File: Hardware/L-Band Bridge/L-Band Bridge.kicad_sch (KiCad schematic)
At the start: 89 parts, among them J1 SMA, J2 SMA, J3 SMA, J4 Conn_02x08_Odd_Even, Q1 MMBT3904, U1 ADP-2-20+, U10 DBTC-17-5LX+, U3 LM358, U4 GALI-52, U5 GALI-52, U6 HMC472ALP4E, U7 ADE-17H+, U9 DBTC-17-5LX+

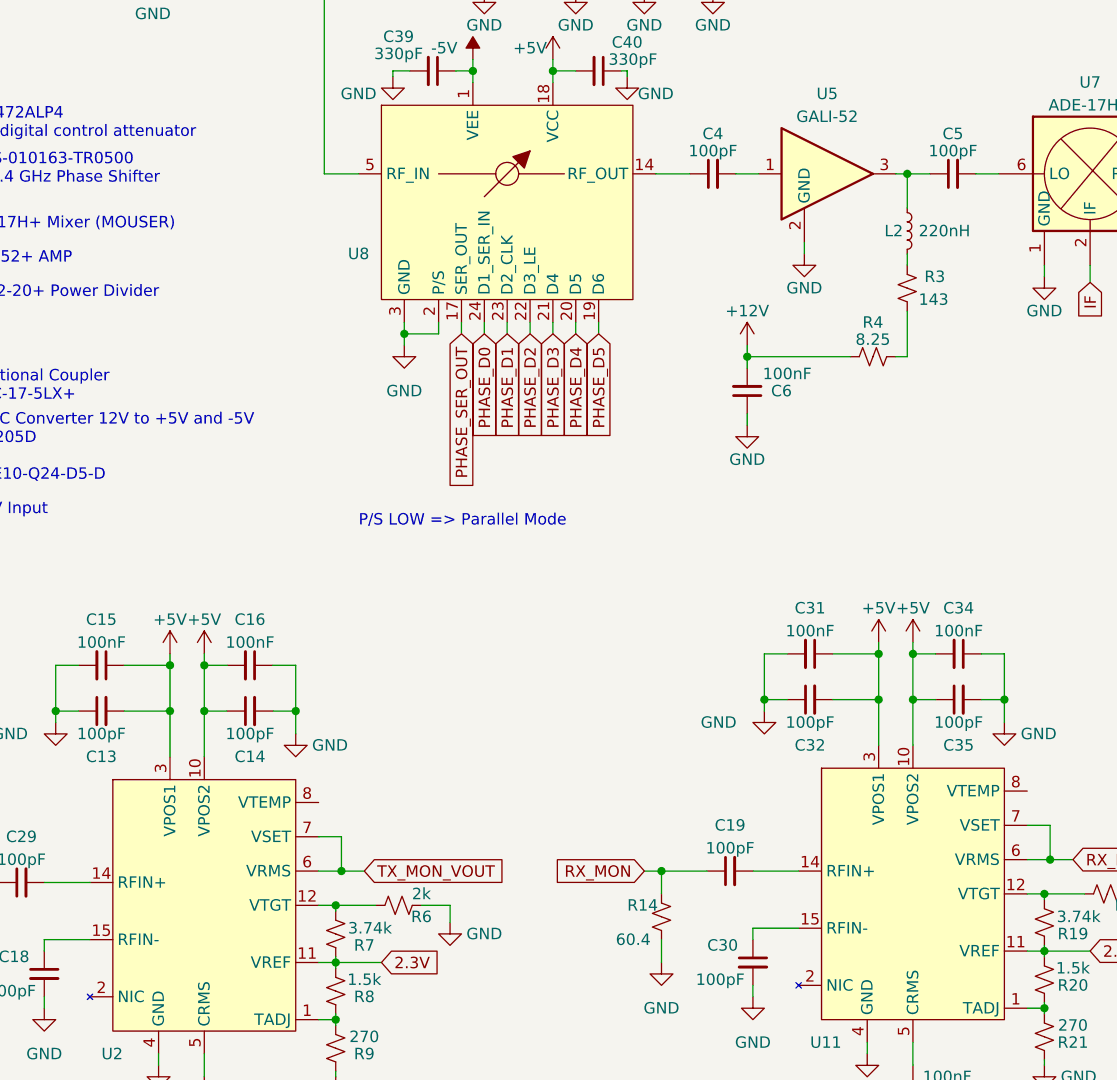
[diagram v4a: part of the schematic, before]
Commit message: Updating L-band bridge schematic
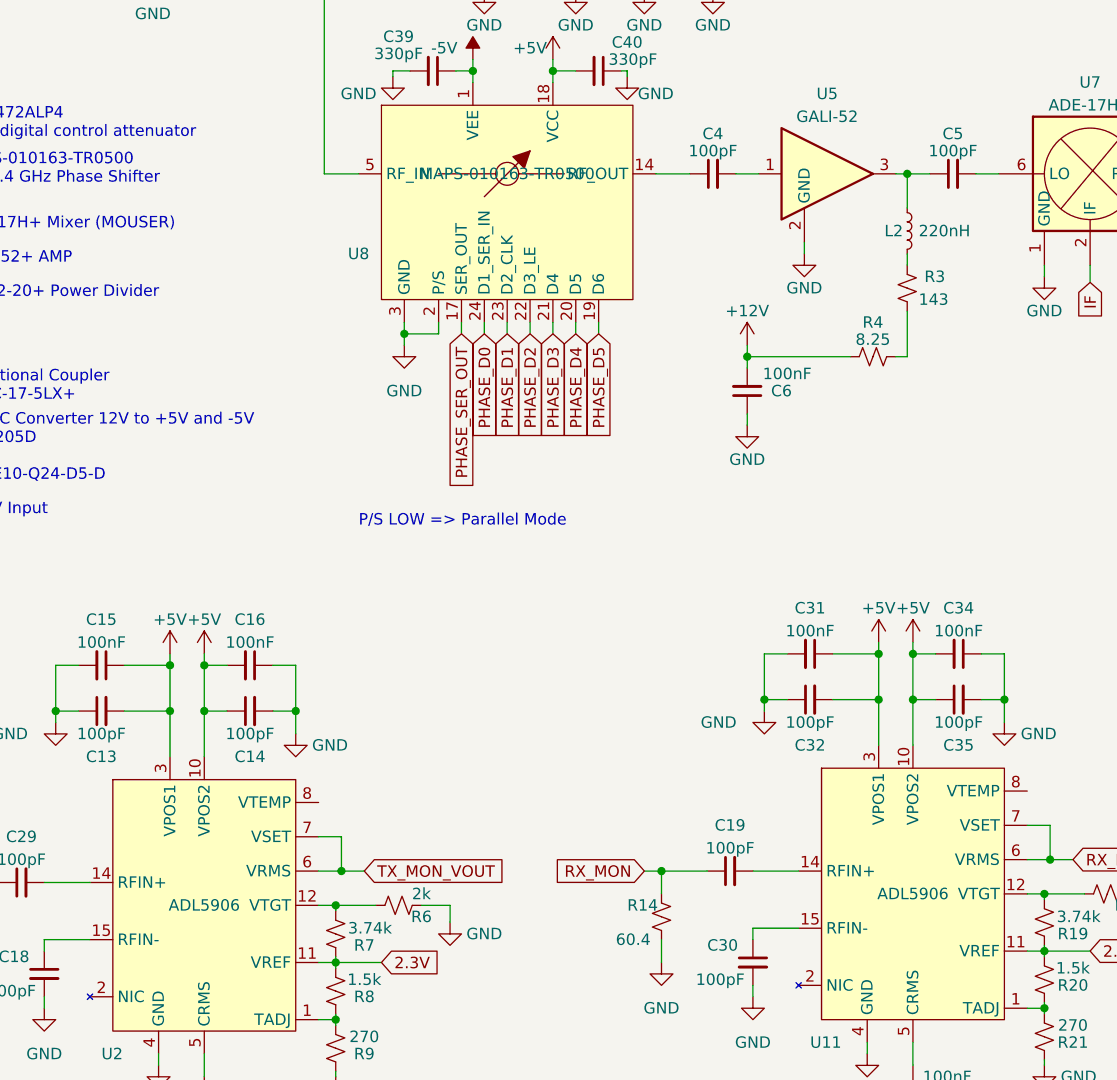
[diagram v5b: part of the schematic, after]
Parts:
- U10, U9: footprint (none) -> _tim-RF-Mini-Circuits:DBTC-17-5LX+
- U11, U2: value ~ -> ADL5906; footprint (none) -> Package_DFN_QFN:QFN-16-1EP_4x4mm_P0.65mm_EP2.1x2.1mm_ThermalVias
- U8: value ~ -> MAPS-010163-TR0500
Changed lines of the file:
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@@
       (effects (font (size 1.27 1.27)))
     )
-    (property "Footprint" "" (at 175.26 56.515 0)
+    (property "Footprint" "_tim-RF-Mini-Circuits:DBTC-17-5LX+" (at 175.26 56.515 0)
       (effects (font (size 1.27 1.27)) hide)
     )
@@
     )
   )
-  (symbol (lib_id "_tim-RF:DBTC-17-5LX+") (at 177.8 81.28 0) (mirror y) (unit 1)
+  (symbol (lib_name "DBTC-17-5LX+_1") (lib_id "_tim-RF:DBTC-17-5LX+") (at 177.8 81.28 0) (mirror y) (unit 1)
     (in_bom yes) (on_board yes) (dnp no)
     (property "Reference" "U10" (at 177.8 76.2 0)
@@
       (effects (font (size 1.27 1.27)))
     )
-    (property "Footprint" "" (at 177.8 95.885 0)
+    (property "Footprint" "_tim-RF-Mini-Circuits:DBTC-17-5LX+" (at 177.8 95.885 0)
       (effects (font (size 1.27 1.27)) hide)
     )
@@
       (effects (font (size 1.27 1.27)))
     )
-    (property "Value" "~" (at 86.36 81.28 0)
+    (property "Value" "MAPS-010163-TR0500" (at 86.36 81.28 0)
       (effects (font (size 1.27 1.27)))
     )
@@
     )
   )
-  (symbol (lib_id "_tim-RF:ADL5906") (at 131.445 161.29 0) (unit 1)
+  (symbol (lib_name "ADL5906_1") (lib_id "_tim-RF:ADL5906") (at 131.445 161.29 0) (unit 1)
     (in_bom yes) (on_board yes) (dnp no)
     (property "Reference" "U11" (at 120.015 177.8 0)
       (effects (font (size 1.27 1.27)) (justify left))
     )
-    (property "Value" "~" (at 131.445 161.29 0)
-      (effects (font (size 1.27 1.27)))
-    )
-    (property "Footprint" "" (at 131.445 161.29 0)
+    (property "Value" "ADL5906" (at 131.445 161.29 0)
+      (effects (font (size 1.27 1.27)))
+    )
+    (property "Footprint" "Package_DFN_QFN:QFN-16-1EP_4x4mm_P0.65mm_EP2.1x2.1mm_ThermalVias" (at 131.445 161.29 0)
       (effects (font (size 1.27 1.27)) hide)
     )
@@
       (effects (font (size 1.27 1.27)) (justify left))
     )
-    (property "Value" "~" (at 52.705 162.56 0)
-      (effects (font (size 1.27 1.27)))
-    )
-    (property "Footprint" "" (at 52.705 162.56 0)
-      (effects (font (size 1.27 1.27)) hide)
-    )
+    (property "Value" "ADL5906" (at 52.705 162.56 0)
+      (effects (font (size 1.27 1.27)))
+    )
+    (property "Footprint" "Package_DFN_QFN:QFN-16-1EP_4x4mm_P0.65mm_EP2.1x2.1mm_ThermalVias" (at 52.705 162.56 0)
+      (effects (font (size 1.27 1.27)) hide)
+    )

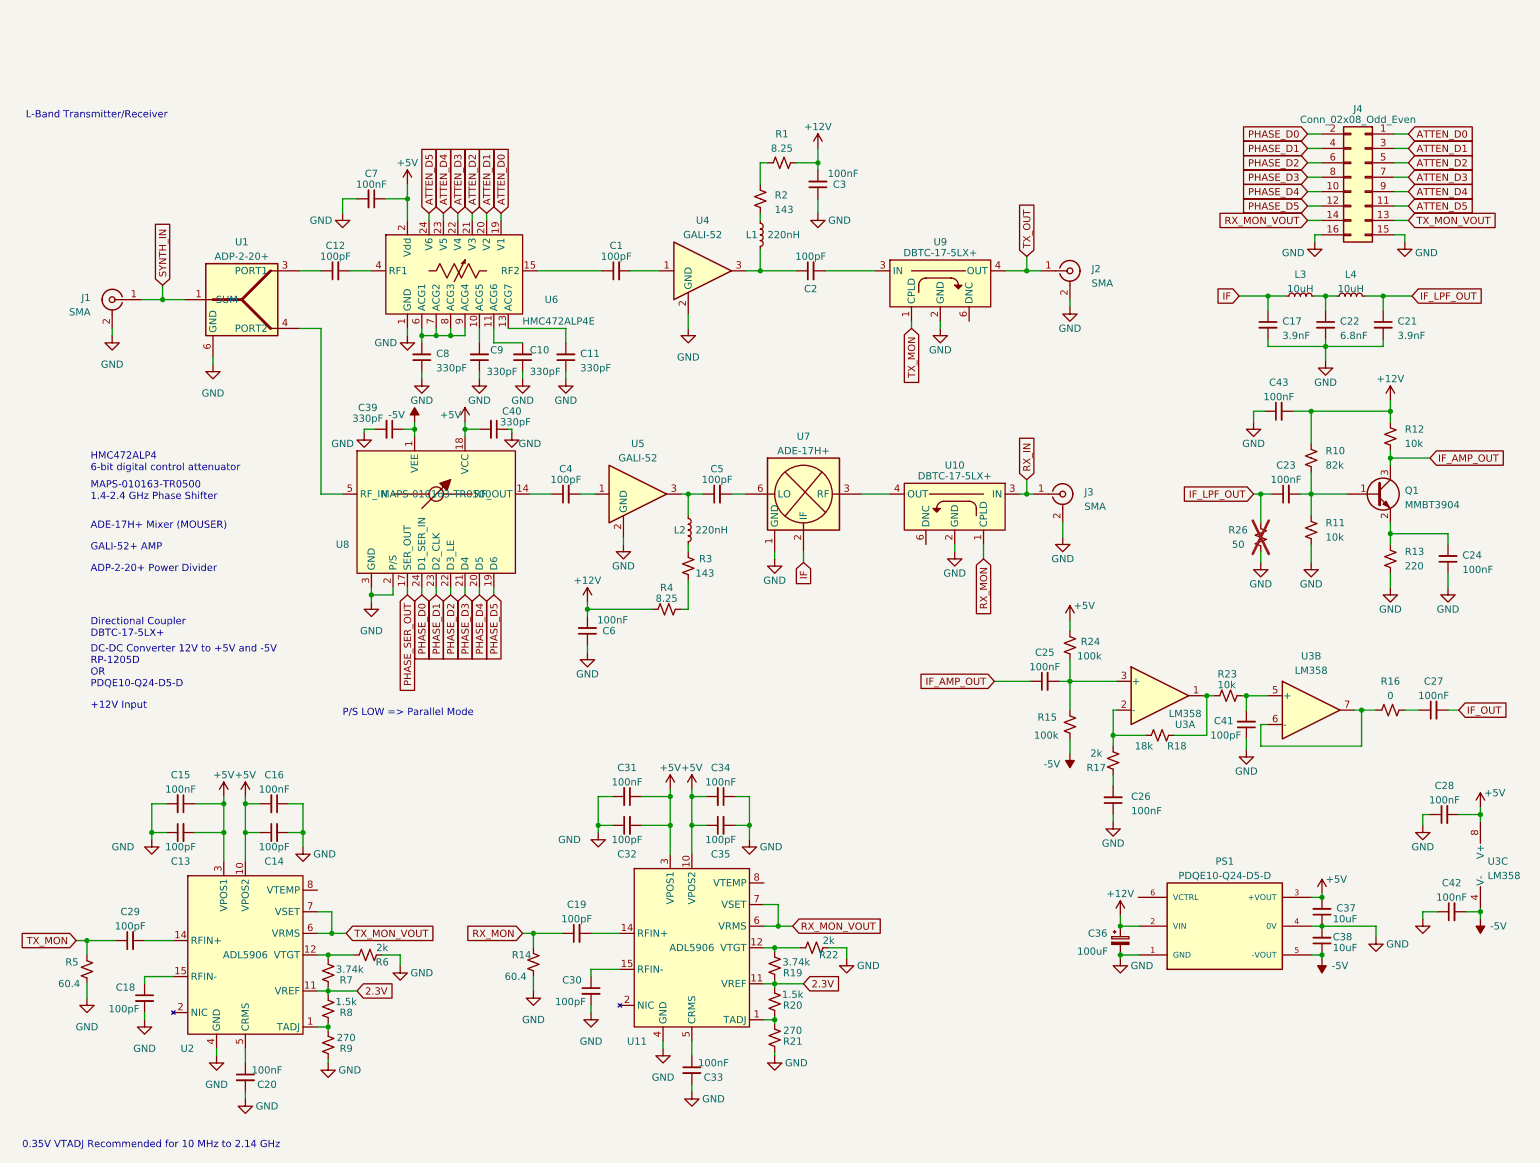
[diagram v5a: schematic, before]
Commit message: Updating Schematic
Removed Power Divider
Removed Op Amp on IF output
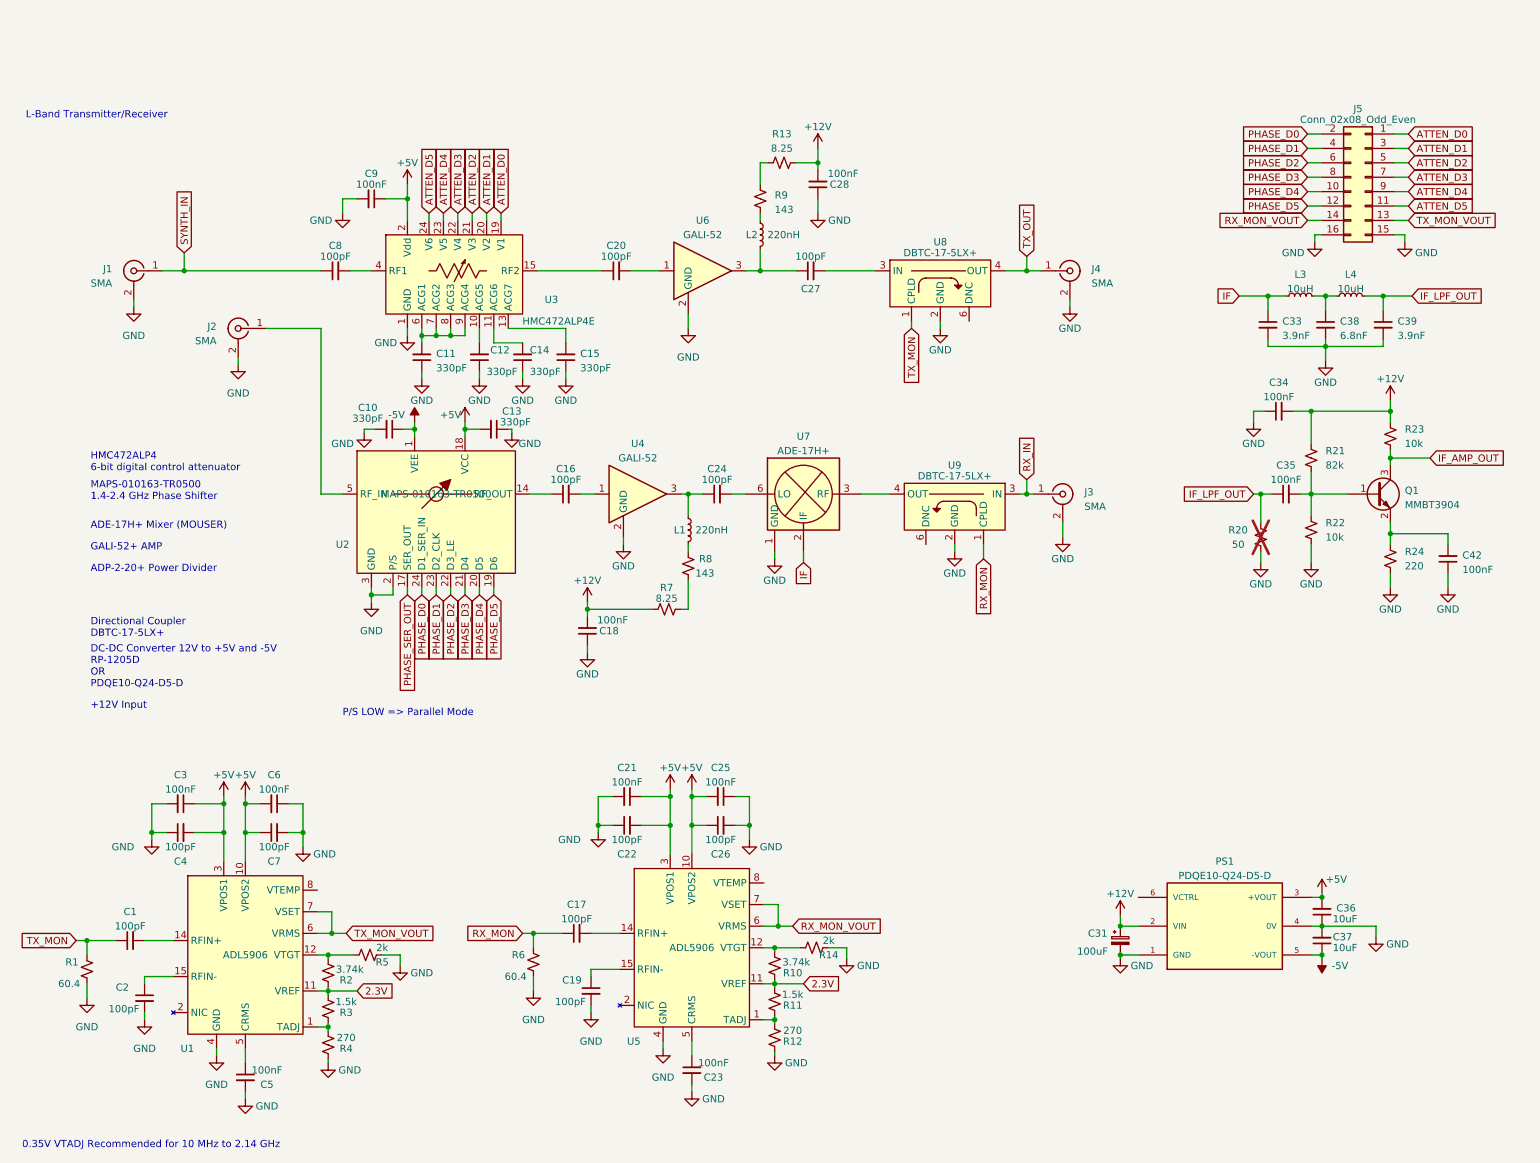
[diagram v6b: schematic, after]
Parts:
- removed C25, C26, C27, C28, C42: 100nF, Capacitor_SMD:C_0402_1005Metric, symbol Device:C_Small
- removed C41: 100pF, Capacitor_SMD:C_0402_1005Metric, symbol Device:C_Small
- removed R15: 100k, Resistor_SMD:R_0402_1005Metric, symbol Device:R_Small_US
- removed R16: 0, Capacitor_SMD:C_0402_1005Metric, symbol Device:R_Small_US
- removed R17: 2k, Capacitor_SMD:C_0402_1005Metric, symbol Device:R_Small_US
- removed R18: 18k, Capacitor_SMD:C_0402_1005Metric, symbol Device:R_Small_US
- removed R23: 10k, Capacitor_SMD:C_0402_1005Metric, symbol Device:R_Small_US
- removed R24: 100k, Capacitor_SMD:C_0402_1005Metric, symbol Device:R_Small_US
- removed U1: ADP-2-20+, RF_Mini-Circuits:Mini-Circuits_CD636_LandPatternPL-035, symbol _tim-RF:ADP-2-20+
- removed U3: LM358, Package_SO:MSOP-8_3x3mm_P0.65mm, symbol Amplifier_Operational:LM358
- added J2: SMA, Connector_Coaxial:SMA_Amphenol_132291_Vertical, symbol Connector:Conn_Coaxial
- renumbered C29 to C1, C39 to C10, C8 to C11, C9 to C12, C40 to C13, C10 to C14, C11 to C15, C4 to C16, C19 to C17, C6 to C18, C30 to C19, C18 to C2, C1 to C20, C31 to C21, C32 to C22, C33 to C23, C5 to C24, C34 to C25, C35 to C26, C2 to C27, C3 to C28, C15 to C3, C36 to C31, C17 to C33, C43 to C34, C23 to C35, C37 to C36, C38 to C37, C22 to C38, C21 to C39, C13 to C4, C24 to C42, C20 to C5, C16 to C6, C14 to C7, C12 to C8, C7 to C9, J2 to J4, J4 to J5, L2 to L1, L1 to L2, R5 to R1, R19 to R10, R20 to R11, R21 to R12, R1 to R13, R22 to R14, R7 to R2, R26 to R20, R10 to R21, R11 to R22, R12 to R23, R13 to R24, R8 to R3, R9 to R4, R6 to R5, R14 to R6, R4 to R7, R3 to R8, R2 to R9, U2 to U1, U8 to U2, U6 to U3, U5 to U4, U11 to U5, U4 to U6, U9 to U8, U10 to U9
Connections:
- net GND: now also J2.2 (Ext)
- net SYNTH_IN: now also C8.1
- net at U2.5 (RF_IN): now also J2.1 (In)
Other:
- moved on the sheet: J1

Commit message: Removing Filter and IF Amp
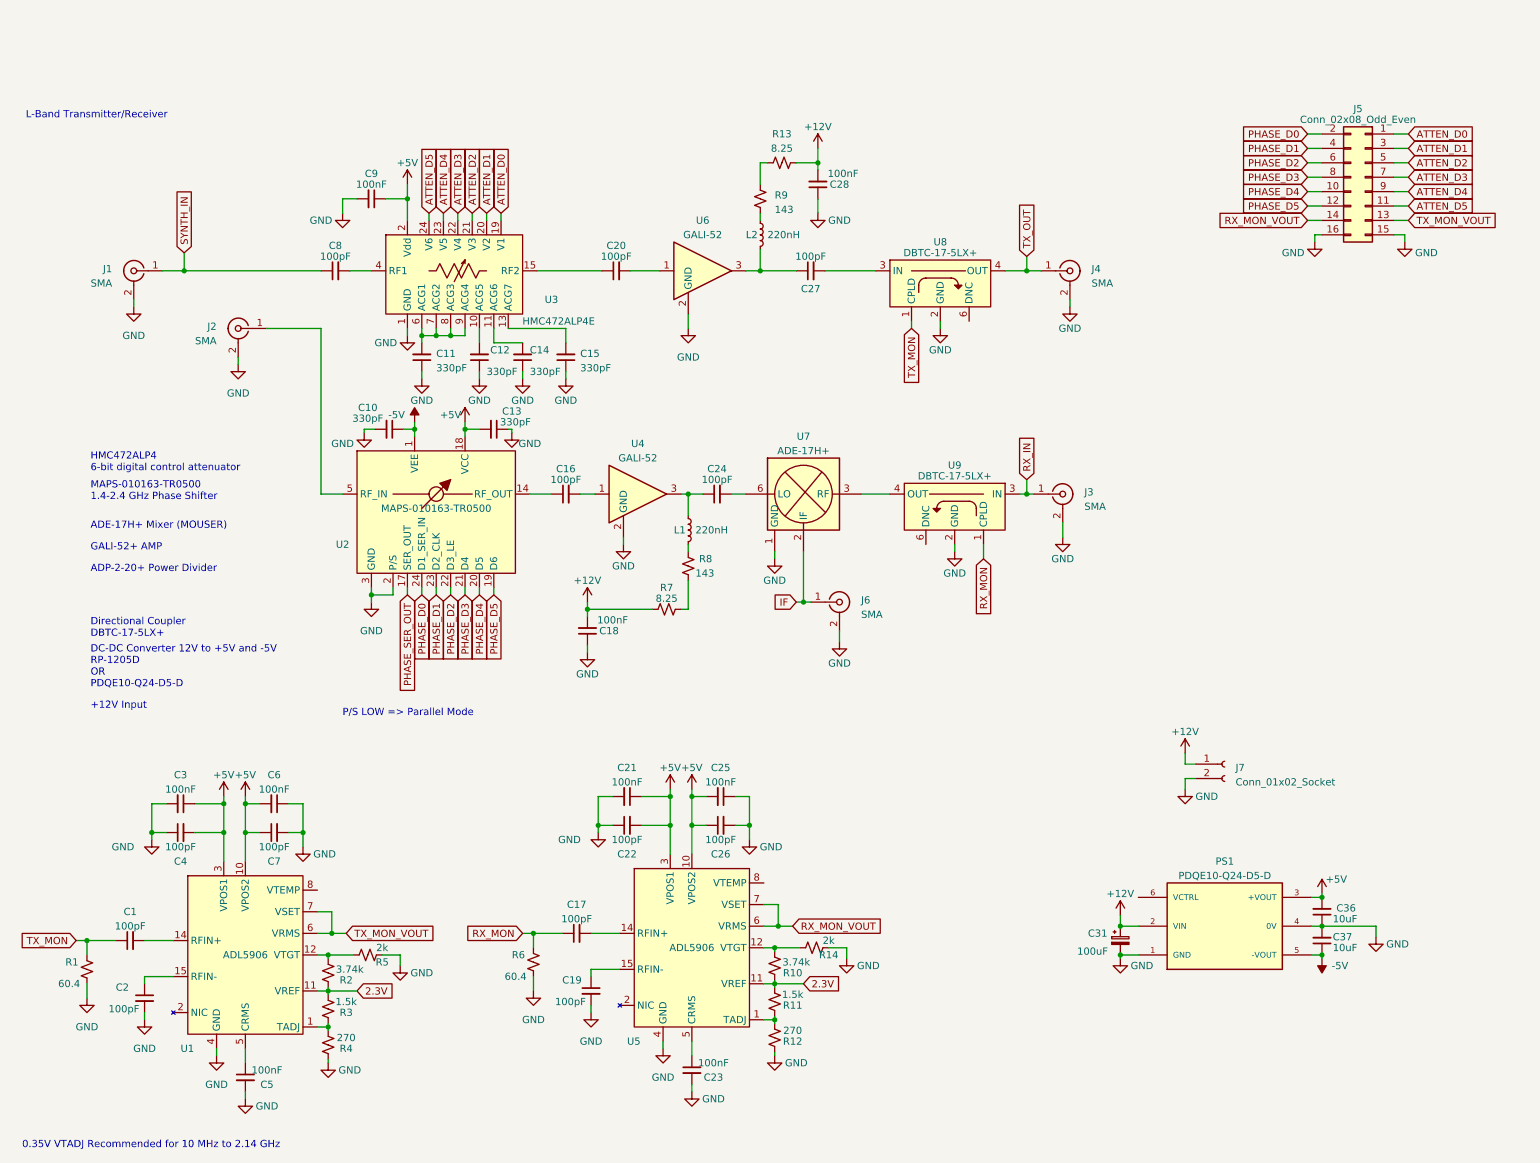
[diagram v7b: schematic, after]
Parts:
- removed C33, C39: 3.9nF, Capacitor_SMD:C_0402_1005Metric, symbol Device:C_Small
- removed C34, C35, C42: 100nF, Capacitor_SMD:C_0402_1005Metric, symbol Device:C_Small
- removed C38: 6.8nF, Capacitor_SMD:C_0402_1005Metric, symbol Device:C_Small
- removed L3, L4: 10uH, symbol Device:L_Small
- removed Q1: MMBT3904, Package_TO_SOT_THT:TO-92_Inline, symbol Transistor_BJT:MMBT3904
- removed R20: 50, Capacitor_SMD:C_0603_1608Metric, symbol Device:R_Small_US
- removed R21: 82k, Resistor_SMD:R_0402_1005Metric, symbol Device:R_Small_US
- removed R22, R23: 10k, Resistor_SMD:R_0402_1005Metric, symbol Device:R_Small_US
- removed R24: 220, Resistor_SMD:R_0402_1005Metric, symbol Device:R_Small_US
- added J6: SMA, Connector_Coaxial:SMA_Amphenol_132291_Vertical, symbol Connector:Conn_Coaxial
- added J7: Conn_01x02_Socket, symbol Connector:Conn_01x02_Socket
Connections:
- net +12V: now also J7.1 (Pin_1)
- net GND: now also J6.2 (Ext), J7.2 (Pin_2)
- net IF: now also J6.1 (In)
